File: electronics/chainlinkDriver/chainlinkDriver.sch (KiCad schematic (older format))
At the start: 70 parts, among them J1 Inputs, J10 Sensor C, J11 Sensor D, J12 Motor E, J13 Motor F, J14 Sensor E, J15 Sensor F, J16 Power, J17 Power, J18 Power, J19 Outputs, J2 Inputs, J20 Outputs, J21 Outputs, J3 Motor A, J4 Inputs, J5 Motor B, J6 Motor C, J7 Motor D, J8 Sensor A, J9 Sensor B, U1 74HC595, U10 TPL7407L, U2 TPL7407L, U3 74HC125, U4 74HC165, U5 74HC595, U6 TPL7407L, U7 74HC595, U8 TPL7407L, U9 74HC595

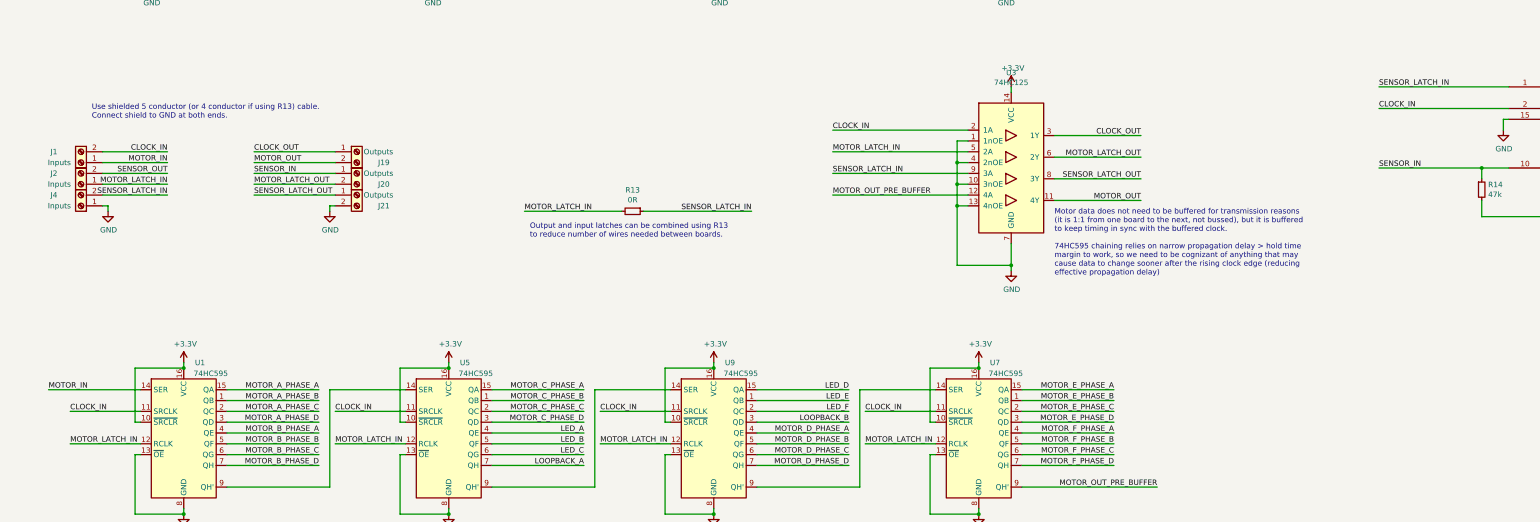
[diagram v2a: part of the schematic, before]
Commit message: Change Chainlink data connections from screw terminals to IDC (#189)
- Replace screw terminals with 2x4 IDC connectors (alternating ground) on Driver, Base, and Tester. Fixes #179
- Change Chainlink Driver Tester to all 1mm pogo pins
- Create new "Buddy" boards for connecting IDC/ribbon cable to T-Display or a breadboard
- Big readme cleanup and reorganization for clarity (hopefully!)
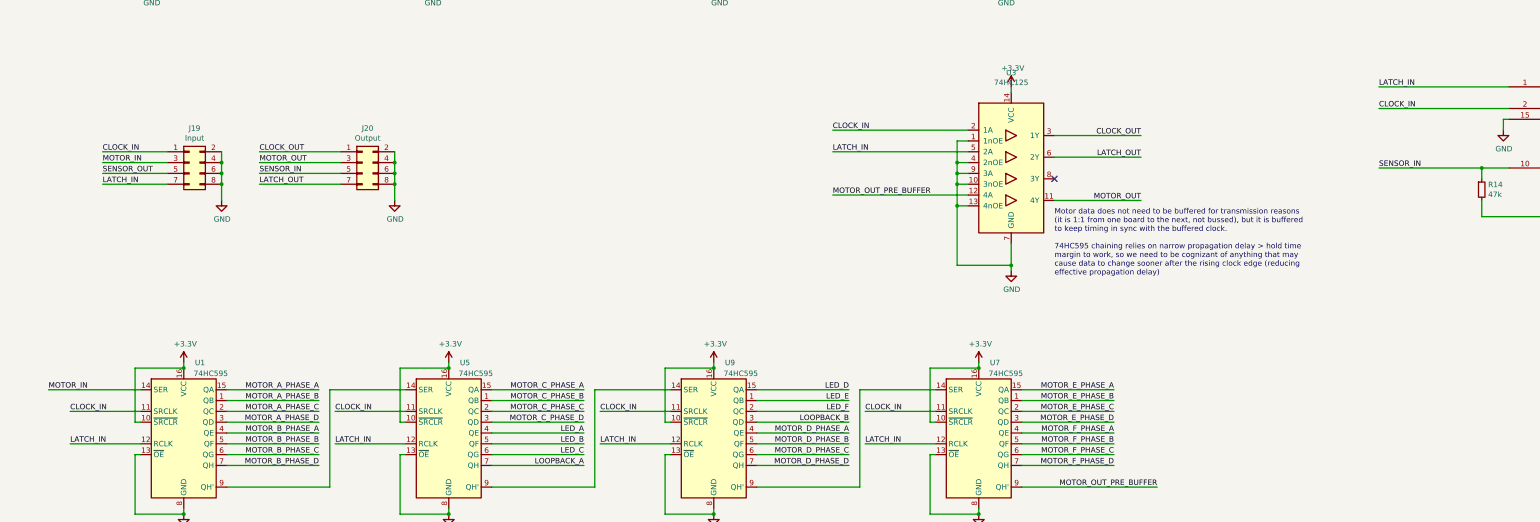
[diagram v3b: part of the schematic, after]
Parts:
- removed J1, J2, J4: Inputs, ScrewTerminals:C8465_WJ500V-5.08-2P, symbol Connector:Screw_Terminal_01x02
- removed J19, J20, J21: Outputs, ScrewTerminals:C8465_WJ500V-5.08-2P, symbol Connector:Screw_Terminal_01x02
- removed R13: 0R, Resistor_SMD:R_0603_1608Metric, symbol Device:R_Small
- added J19: Input, ModifiedSymbols:IDC-Header_2x04_P2.54mm_Vertical, symbol Connector_Generic:Conn_02x04_Odd_Even
- added J20: Output, ModifiedSymbols:IDC-Header_2x04_P2.54mm_Vertical, symbol Connector_Generic:Conn_02x04_Odd_Even
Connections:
- net CLOCK_IN: now also J19.1 (Pin_1)
- net CLOCK_OUT: now also J20.1 (Pin_1)
- net GND: now also U3.9 (3A), J19.2 (Pin_2), J19.4 (Pin_4), J19.6 (Pin_6), J19.8 (Pin_8), J20.2 (Pin_2), J20.4 (Pin_4), J20.6 (Pin_6), J20.8 (Pin_8)
- net MOTOR_IN: now also J19.3 (Pin_3)
- net MOTOR_OUT: now also J20.3 (Pin_3)
- net SENSOR_IN: now also J20.5 (Pin_5)
- net SENSOR_OUT: now also J19.5 (Pin_5)
- net MOTOR_LATCH_IN renamed LATCH_IN
- net LATCH_IN: now also U4.1 (~LD), J19.7 (Pin_7)
- net MOTOR_LATCH_OUT renamed LATCH_OUT
- net LATCH_OUT: now also J20.7 (Pin_7)
- removed net SENSOR_LATCH_IN: U3.9 (3A), U4.1 (~LD)
- net SENSOR_LATCH_OUT: no longer names the net of U3.8 (3Y)
- no-connect marks 10 -> 11
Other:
- note removed: "Output and input latches can be combined using R13\nto reduce number of wires needed between boards."
- note removed: "Use shielded 5 conductor (or 4 conductor if using R13) cable.\nConnect shield to GND at both ends."
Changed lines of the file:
@@
 	1800 9100 1150 9100
 Text Label 1150 9100 0    50   ~ 0
-MOTOR_LATCH_IN
+LATCH_IN
 $Comp
 L power:GND #PWR08
@@
 	4250 9100 3600 9100
 Text Label 3600 9100 0    50   ~ 0
-MOTOR_LATCH_IN
+LATCH_IN
 $Comp
 L power:GND #PWR027
@@
 	9150 9100 8500 9100
 Text Label 8500 9100 0    50   ~ 0
-MOTOR_LATCH_IN
+LATCH_IN
 $Comp
 L power:GND #PWR033
@@
 	15050 5250 15050 5300
 NoConn ~ 15650 6650
-Text Label 13250 5800 0    50   ~ 0
-SENSOR_LATCH_IN
 Text Label 13250 6000 0    50   ~ 0
 CLOCK_IN
@@
 L power:GND #PWR04
 U 1 1 60FBE6C2
-P 1500 6950
-F 0 "#PWR04" H 1500 6700 50  0001 C CNN
-F 1 "GND" H 1505 6777 50  0000 C CNN
-F 2 "" H 1500 6950 50  0001 C CNN
-F 3 "" H 1500 6950 50  0001 C CNN
-	1    1500 6950
+P 2550 6850
+F 0 "#PWR04" H 2550 6600 50  0001 C CNN
+F 1 "GND" H 2555 6677 50  0000 C CNN
+F 2 "" H 2550 6850 50  0001 C CNN
+F 3 "" H 2550 6850 50  0001 C CNN
+	1    2550 6850
 	1    0    0    -1
 $EndComp
@@
 L power:GND #PWR020
 U 1 1 60FBEBB8
-P 3550 6950
-F 0 "#PWR020" H 3550 6700 50  0001 C CNN
-F 1 "GND" H 3555 6777 50  0000 C CNN
-F 2 "" H 3550 6950 50  0001 C CNN
-F 3 "" H 3550 6950 50  0001 C CNN
-	1    3550 6950
-	1    0    0    -1
-$EndComp
-Wire Wire Line
-	1450 6900 1500 6900
-Wire Wire Line
-	1500 6900 1500 6950
-Wire Wire Line
-	3600 6900 3550 6900
-Wire Wire Line
-	3550 6900 3550 6950
-Wire Wire Line
-	1450 6400 2050 6400
-Wire Wire Line
-	1450 6700 2050 6700
-Wire Wire Line
-	1450 6500 2050 6500
-Wire Wire Line
-	1450 6600 2050 6600
-Text Label 2050 6400 2    50   ~ 0
-CLOCK_IN
-Text Label 2050 6700 2    50   ~ 0
-MOTOR_LATCH_IN
-Text Label 2050 6500 2    50   ~ 0
-MOTOR_IN
-Text Label 2050 6600 2    50   ~ 0
-SENSOR_OUT
-Text Label 2850 6400 0    50   ~ 0
+P 4150 6850
+F 0 "#PWR020" H 4150 6600 50  0001 C CNN
+F 1 "GND" H 4155 6677 50  0000 C CNN
+F 2 "" H 4150 6850 50  0001 C CNN
+F 3 "" H 4150 6850 50  0001 C CNN
+	1    4150 6850
+	1    0    0    -1
+$EndComp
+Text Label 2900 6400 0    50   ~ 0
 CLOCK_OUT
-Text Label 2850 6700 0    50   ~ 0
-MOTOR_LATCH_OUT
-Text Label 2850 6500 0    50   ~ 0
+Text Label 2900 6700 0    50   ~ 0
+LATCH_OUT
+Text Label 2900 6500 0    50   ~ 0
 MOTOR_OUT
-Text Label 2850 6600 0    50   ~ 0
+Text Label 2900 6600 0    50   ~ 0
 SENSOR_IN
 $Comp
@@
 	6700 9100 6050 9100
 Text Label 6050 9100 0    50   ~ 0
-MOTOR_LATCH_IN
+LATCH_IN
 $Comp
 L power:GND #PWR040
@@
 Text Label 8200 6200 0    50   ~ 0
 CLOCK_IN
-Text Label 8200 6400 0    50   ~ 0
-MOTOR_LATCH_IN
 Text Label 8200 6800 0    50   ~ 0
 MOTOR_OUT_PRE_BUFFER
 Text Label 11050 6250 2    50   ~ 0
 CLOCK_OUT
-Text Label 11050 6450 2    50   ~ 0
-MOTOR_LATCH_OUT
 Text Label 11050 6850 2    50   ~ 0
 MOTOR_OUT
@@
 	9450 6500 9350 6500
 Connection ~ 9350 6500
-Wire Wire Line
-	9350 6500 9350 6700
 Wire Wire Line
 	9350 6700 9450 6700
@@
 	1    0    0    -1
 $EndComp
-Text Label 8200 6600 0    50   ~ 0
-SENSOR_LATCH_IN
-Wire Wire Line
-	8200 6600 9450 6600
 Wire Wire Line
 	10250 6250 11050 6250
@@
 Wire Wire Line
 	10250 6850 11050 6850
-Text Label 11050 6650 2    50   ~ 0
-SENSOR_LATCH_OUT
-Wire Wire Line
-	10250 6650 11050 6650
-Wire Wire Line
-	1450 6800 2050 6800
-Text Label 2050 6800 2    50   ~ 0
-SENSOR_LATCH_IN
-Text Label 2850 6800 0    50   ~ 0
-SENSOR_LATCH_OUT
-Wire Wire Line
-	2850 6400 3600 6400
-Wire Wire Line
-	2850 6700 3600 6700
-Wire Wire Line
-	2850 6800 3600 6800
-Wire Wire Line
-	2850 6500 3600 6500
-Wire Wire Line
-	2850 6600 3600 6600
-Text Label 5350 6950 0    50   ~ 0
-MOTOR_LATCH_IN
-Text Label 7450 6950 2    50   ~ 0
-SENSOR_LATCH_IN
-Wire Wire Line
-	5350 6950 6250 6950
-Wire Wire Line
-	6450 6950 7450 6950
-$Comp
-L Device:R_Small R13
-U 1 1 60F91757
-P 6350 6950
-F 0 "R13" V 6154 6950 50  0000 C CNN
-F 1 "0R" V 6245 6950 50  0000 C CNN
-F 2 "Resistor_SMD:R_0603_1608Metric" H 6350 6950 50  0001 C CNN
-F 3 "~" H 6350 6950 50  0001 C CNN
-F 4 "C21189" V 6350 6950 50  0001 C CNN "LCSC"
-	1    6350 6950
-	0    1    1    0
-$EndComp
+Wire Wire Line
+	2900 6400 3650 6400
+Wire Wire Line
+	2900 6700 3650 6700
+Wire Wire Line
+	2900 6500 3650 6500
+Wire Wire Line
+	2900 6600 3650 6600
 Wire Wire Line
 	9450 6900 9350 6900
@@
 Text Notes 10250 4600 0    50   ~ 0
 Do not use O7 on TPL7407L\n(see note above)
-Text Notes 5400 7200 0    50   ~ 0
-Output and input latches can be combined using R13\nto reduce number of wires needed between boards.
 Text Notes 10250 7550 0    50   ~ 0
 Motor data does not need to be buffered for transmission reasons\n(it is 1:1 from one board to the next, not bussed), but it is buffered\nto keep timing in sync with the buffered clock.\n\n74HC595 chaining relies on narrow propagation delay > hold time\nmargin to work, so we need to be cognizant of anything that may\ncause data to change sooner after the rising clock edge (reducing\neffective propagation delay)
-Text Notes 1350 6100 0    50   ~ 0
-Use shielded 5 conductor (or 4 conductor if using R13) cable.\nConnect shield to GND at both ends.
 $Comp
 L Connector:Screw_Terminal_01x02 J16
@@
 $EndComp
 $Comp
-L Connector:Screw_Terminal_01x02 J4
-U 1 1 605198F6
-P 1250 6900
-F 0 "J4" H 1500 6800 50  0000 C CNN
-F 1 "Inputs" H 1450 6900 50  0000 C CNN
-F 2 "ScrewTerminals:C8465_WJ500V-5.08-2P" H 1250 6900 50  0001 C CNN
-F 3 "~" H 1250 6900 50  0001 C CNN
-F 4 "C8465" H 1250 6900 50  0001 C CNN "LCSC"
-F 5 "2.40;0;0" H 1250 6900 50  0001 C CNN "JLCPCB_CORRECTION"
-	1    1250 6900
-	-1   0    0    1
-$EndComp
-$Comp
-L Connector:Screw_Terminal_01x02 J2
-U 1 1 6055C477
-P 1250 6700
-F 0 "J2" H 1500 6600 50  0000 C CNN
-F 1 "Inputs" H 1450 6700 50  0000 C CNN
-F 2 "ScrewTerminals:C8465_WJ500V-5.08-2P" H 1250 6700 50  0001 C CNN
-F 3 "~" H 1250 6700 50  0001 C CNN
-F 4 "C8465" H 1250 6700 50  0001 C CNN "LCSC"
-F 5 "2.40;0;0" H 1250 6700 50  0001 C CNN "JLCPCB_CORRECTION"
-	1    1250 6700
-	-1   0    0    1
-$EndComp
-$Comp
-L Connector:Screw_Terminal_01x02 J1
-U 1 1 6055C6FC
-P 1250 6500
-F 0 "J1" H 1500 6400 50  0000 C CNN
-F 1 "Inputs" H 1450 6500 50  0000 C CNN
-F 2 "ScrewTerminals:C8465_WJ500V-5.08-2P" H 1250 6500 50  0001 C CNN
-F 3 "~" H 1250 6500 50  0001 C CNN
-F 4 "C8465" H 1250 6500 50  0001 C CNN "LCSC"
-F 5 "2.40;0;0" H 1250 6500 50  0001 C CNN "JLCPCB_CORRECTION"
-	1    1250 6500
-	-1   0    0    1
-$EndComp
-$Comp
-L Connector:Screw_Terminal_01x02 J19
-U 1 1 6055DB99
-P 3800 6400
-F 0 "J19" H 4050 6300 50  0000 C CNN
-F 1 "Outputs" H 4000 6400 50  0000 C CNN
-F 2 "ScrewTerminals:C8465_WJ500V-5.08-2P" H 3800 6400 50  0001 C CNN
-F 3 "~" H 3800 6400 50  0001 C CNN
-F 4 "C8465" H 3800 6400 50  0001 C CNN "LCSC"
-F 5 "2.40;0;0" H 3800 6400 50  0001 C CNN "JLCPCB_CORRECTION"
-	1    3800 6400
-	1    0    0    -1
-$EndComp
-$Comp
-L Connector:Screw_Terminal_01x02 J20
-U 1 1 6056062F
-P 3800 6600
-F 0 "J20" H 4050 6500 50  0000 C CNN
-F 1 "Outputs" H 4000 6600 50  0000 C CNN
-F 2 "ScrewTerminals:C8465_WJ500V-5.08-2P" H 3800 6600 50  0001 C CNN
-F 3 "~" H 3800 6600 50  0001 C CNN
-F 4 "C8465" H 3800 6600 50  0001 C CNN "LCSC"
-F 5 "2.40;0;0" H 3800 6600 50  0001 C CNN "JLCPCB_CORRECTION"
-	1    3800 6600
-	1    0    0    -1
-$EndComp
-$Comp
-L Connector:Screw_Terminal_01x02 J21
-U 1 1 60560DD4
-P 3800 6800
-F 0 "J21" H 4050 6700 50  0000 C CNN
-F 1 "Outputs" H 4000 6800 50  0000 C CNN
-F 2 "ScrewTerminals:C8465_WJ500V-5.08-2P" H 3800 6800 50  0001 C CNN
-F 3 "~" H 3800 6800 50  0001 C CNN
-F 4 "C8465" H 3800 6800 50  0001 C CNN "LCSC"
-F 5 "2.40;0;0" H 3800 6800 50  0001 C CNN "JLCPCB_CORRECTION"
-	1    3800 6800
-	1    0    0    -1
-$EndComp
-$Comp
 L Device:R_Small R14
 U 1 1 60866A83
@@
 	14200 7000 15050 7000
 Connection ~ 15050 7000
+Text Label 1450 6600 0    50   ~ 0
+SENSOR_OUT
+Text Label 1450 6500 0    50   ~ 0
+MOTOR_IN
+Text Label 1450 6700 0    50   ~ 0
+LATCH_IN
+Text Label 1450 6400 0    50   ~ 0
+CLOCK_IN
+Wire Wire Line
+	1450 6600 2050 6600
+Wire Wire Line
+	1450 6500 2050 6500
+Wire Wire Line
+	1450 6700 2050 6700
+Wire Wire Line
+	1450 6400 2050 6400
+$Comp
+L Connector_Generic:Conn_02x04_Odd_Even J19
+U 1 1 61861E9F
+P 2250 6500
+F 0 "J19" H 2300 6817 50  0000 C CNN
+F 1 "Input" H 2300 6726 50  0000 C CNN
+F 2 "ModifiedSymbols:IDC-Header_2x04_P2.54mm_Vertical" H 2250 6500 50  0001 C CNN
+F 3 "~" H 2250 6500 50  0001 C CNN
+	1    2250 6500
+	1    0    0    -1
+$EndComp
+Wire Wire Line
+	2550 6400 2550 6500
+Connection ~ 2550 6500
+Wire Wire Line
+	2550 6500 2550 6600
+Connection ~ 2550 6600
+Wire Wire Line
+	2550 6600 2550 6700
+Connection ~ 2550 6700
+Wire Wire Line
+	2550 6700 2550 6850
+$Comp
+L Connector_Generic:Conn_02x04_Odd_Even J20
+U 1 1 618D5E87
+P 3850 6500
+F 0 "J20" H 3900 6817 50  0000 C CNN
+F 1 "Output" H 3900 6726 50  0000 C CNN
+F 2 "ModifiedSymbols:IDC-Header_2x04_P2.54mm_Vertical" H 3850 6500 50  0001 C CNN
+F 3 "~" H 3850 6500 50  0001 C CNN
+	1    3850 6500
+	1    0    0    -1
+$EndComp
+Wire Wire Line
+	4150 6850 4150 6700
+Connection ~ 4150 6500
+Wire Wire Line
+	4150 6500 4150 6400
+Connection ~ 4150 6600
+Wire Wire Line
+	4150 6600 4150 6500
+Connection ~ 4150 6700
+Wire Wire Line
+	4150 6700 4150 6600
+Text Label 8200 6400 0    50   ~ 0
+LATCH_IN
+Text Label 11050 6450 2    50   ~ 0
+LATCH_OUT
+NoConn ~ 10250 6650
+Wire Wire Line
+	9450 6600 9350 6600
+Wire Wire Line
+	9350 6500 9350 6600
+Wire Wire Line
+	9350 6600 9350 6700
+Connection ~ 9350 6600
+Text Label 13250 5800 0    50   ~ 0
+LATCH_IN
 $EndSCHEMATC

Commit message: Add JLC alternatives for TPL7407L (ULN2003A) and screw terminal
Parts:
- J16, J17, J18: footprint ScrewTerminals:C8465_WJ500V-5.08-2P -> ScrewTerminals:Generic-5.08-2P; LCSC_ALT_SCREW_DIBO (none) -> C395868
- U10, U2, U6, U8: LCSC_ALT_ULN2003A (none) -> C7512
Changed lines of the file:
@@
 F 3 "~" H 2000 3900 50  0001 C CNN
 F 4 "C139663" H 1900 4100 50  0001 C CNN "LCSC"
-F 5 "0;0;-90" H 1900 4100 50  0001 C CNN "JLCPCB_CORRECTION"
+F 5 "C7512" H 1900 4100 50  0001 C CNN "LCSC_ALT_ULN2003A"
+F 6 "0;0;-90" H 1900 4100 50  0001 C CNN "JLCPCB_CORRECTION"
 	1    1900 4100
 	1    0    0    -1
@@
 F 3 "~" H 4600 3900 50  0001 C CNN
 F 4 "C139663" H 4500 4100 50  0001 C CNN "LCSC"
-F 5 "0;0;-90" H 4500 4100 50  0001 C CNN "JLCPCB_CORRECTION"
+F 5 "C7512" H 4500 4100 50  0001 C CNN "LCSC_ALT_ULN2003A"
+F 6 "0;0;-90" H 4500 4100 50  0001 C CNN "JLCPCB_CORRECTION"
 	1    4500 4100
 	1    0    0    -1
@@
 F 3 "~" H 9900 3900 50  0001 C CNN
 F 4 "C139663" H 9800 4100 50  0001 C CNN "LCSC"
-F 5 "0;0;-90" H 9800 4100 50  0001 C CNN "JLCPCB_CORRECTION"
+F 5 "C7512" H 9800 4100 50  0001 C CNN "LCSC_ALT_ULN2003A"
+F 6 "0;0;-90" H 9800 4100 50  0001 C CNN "JLCPCB_CORRECTION"
 	1    9800 4100
 	1    0    0    -1
@@
 F 3 "~" H 7250 3900 50  0001 C CNN
 F 4 "C139663" H 7150 4100 50  0001 C CNN "LCSC"
-F 5 "0;0;-90" H 7150 4100 50  0001 C CNN "JLCPCB_CORRECTION"
+F 5 "C7512" H 7150 4100 50  0001 C CNN "LCSC_ALT_ULN2003A"
+F 6 "0;0;-90" H 7150 4100 50  0001 C CNN "JLCPCB_CORRECTION"
 	1    7150 4100
 	1    0    0    -1
@@
 F 0 "J16" H 1680 892 50  0000 L CNN
 F 1 "Power" H 1680 801 50  0000 L CNN
-F 2 "ScrewTerminals:C8465_WJ500V-5.08-2P" H 1600 900 50  0001 C CNN
+F 2 "ScrewTerminals:Generic-5.08-2P" H 1600 900 50  0001 C CNN
 F 3 "~" H 1600 900 50  0001 C CNN
 F 4 "C8465" H 1600 900 50  0001 C CNN "LCSC"
-F 5 "2.40;0;0" H 1600 900 50  0001 C CNN "JLCPCB_CORRECTION"
+F 5 "C395868" H 1600 900 50  0001 C CNN "LCSC_ALT_SCREW_DIBO"
+F 6 "2.40;0;0" H 1600 900 50  0001 C CNN "JLCPCB_CORRECTION"
 	1    1600 900
 	1    0    0    -1
@@
 F 0 "J17" H 1680 1092 50  0000 L CNN
 F 1 "Power" H 1680 1001 50  0000 L CNN
-F 2 "ScrewTerminals:C8465_WJ500V-5.08-2P" H 1600 1100 50  0001 C CNN
+F 2 "ScrewTerminals:Generic-5.08-2P" H 1600 1100 50  0001 C CNN
 F 3 "~" H 1600 1100 50  0001 C CNN
 F 4 "C8465" H 1600 1100 50  0001 C CNN "LCSC"
-F 5 "2.40;0;0" H 1600 1100 50  0001 C CNN "JLCPCB_CORRECTION"
+F 5 "C395868" H 1600 1100 50  0001 C CNN "LCSC_ALT_SCREW_DIBO"
+F 6 "2.40;0;0" H 1600 1100 50  0001 C CNN "JLCPCB_CORRECTION"
 	1    1600 1100
 	1    0    0    -1
@@
 F 0 "J18" H 1680 1292 50  0000 L CNN
 F 1 "Power" H 1680 1201 50  0000 L CNN
-F 2 "ScrewTerminals:C8465_WJ500V-5.08-2P" H 1600 1300 50  0001 C CNN
+F 2 "ScrewTerminals:Generic-5.08-2P" H 1600 1300 50  0001 C CNN
 F 3 "~" H 1600 1300 50  0001 C CNN
 F 4 "C8465" H 1600 1300 50  0001 C CNN "LCSC"
-F 5 "2.40;0;0" H 1600 1300 50  0001 C CNN "JLCPCB_CORRECTION"
+F 5 "C395868" H 1600 1300 50  0001 C CNN "LCSC_ALT_SCREW_DIBO"
+F 6 "2.40;0;0" H 1600 1300 50  0001 C CNN "JLCPCB_CORRECTION"
 	1    1600 1300
 	1    0    0    -1
